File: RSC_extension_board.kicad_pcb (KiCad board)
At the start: 2 copper layers, 35 parts, among them J1 Conn_01x03, J10 Conn_01x02, J13 Conn_01x03, J14 500SSP1S2M2QEA, J16 Conn_01x10, J2 Conn_01x03, J3 Raspberry_Pi_4, J4 Conn_01x04, J5 Conn_01x03, J6 Conn_01x02, J7 Conn_01x03, J8 PRT-14417, J9 USB_C_Receptacle_PowerOnly_6P, Q1 BSS138, Q2 2N7002-7-F, U1 USBLC6-2SC6

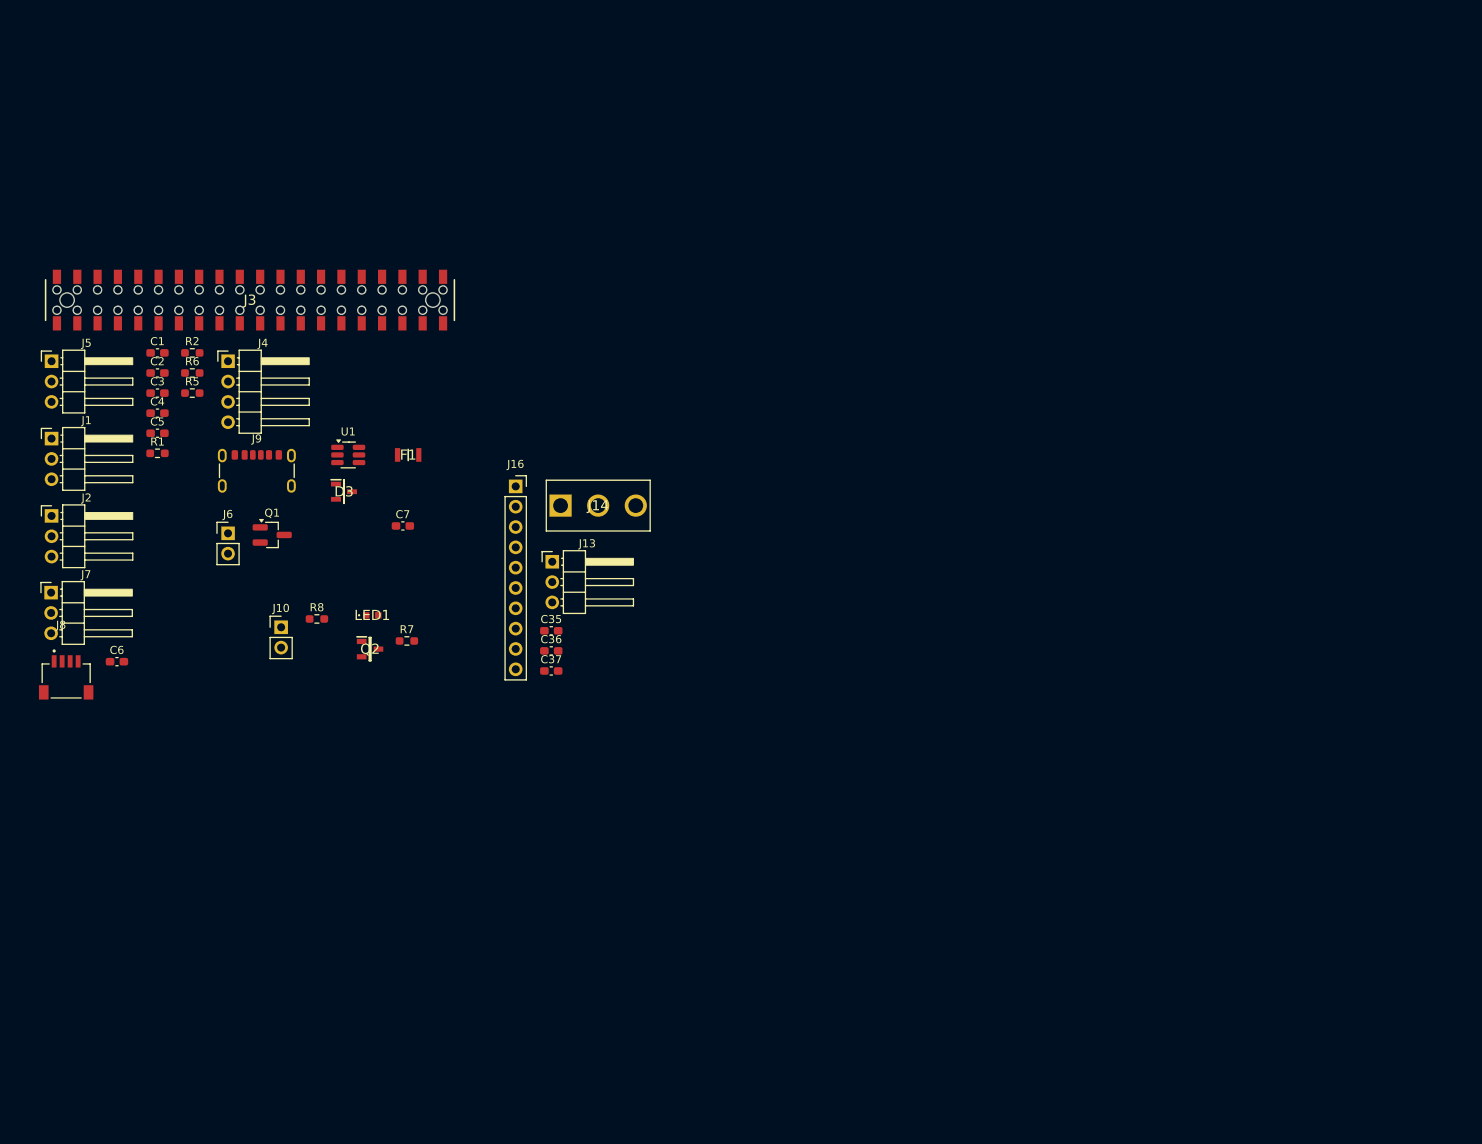
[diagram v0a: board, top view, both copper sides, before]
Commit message: annotation and pcb outline
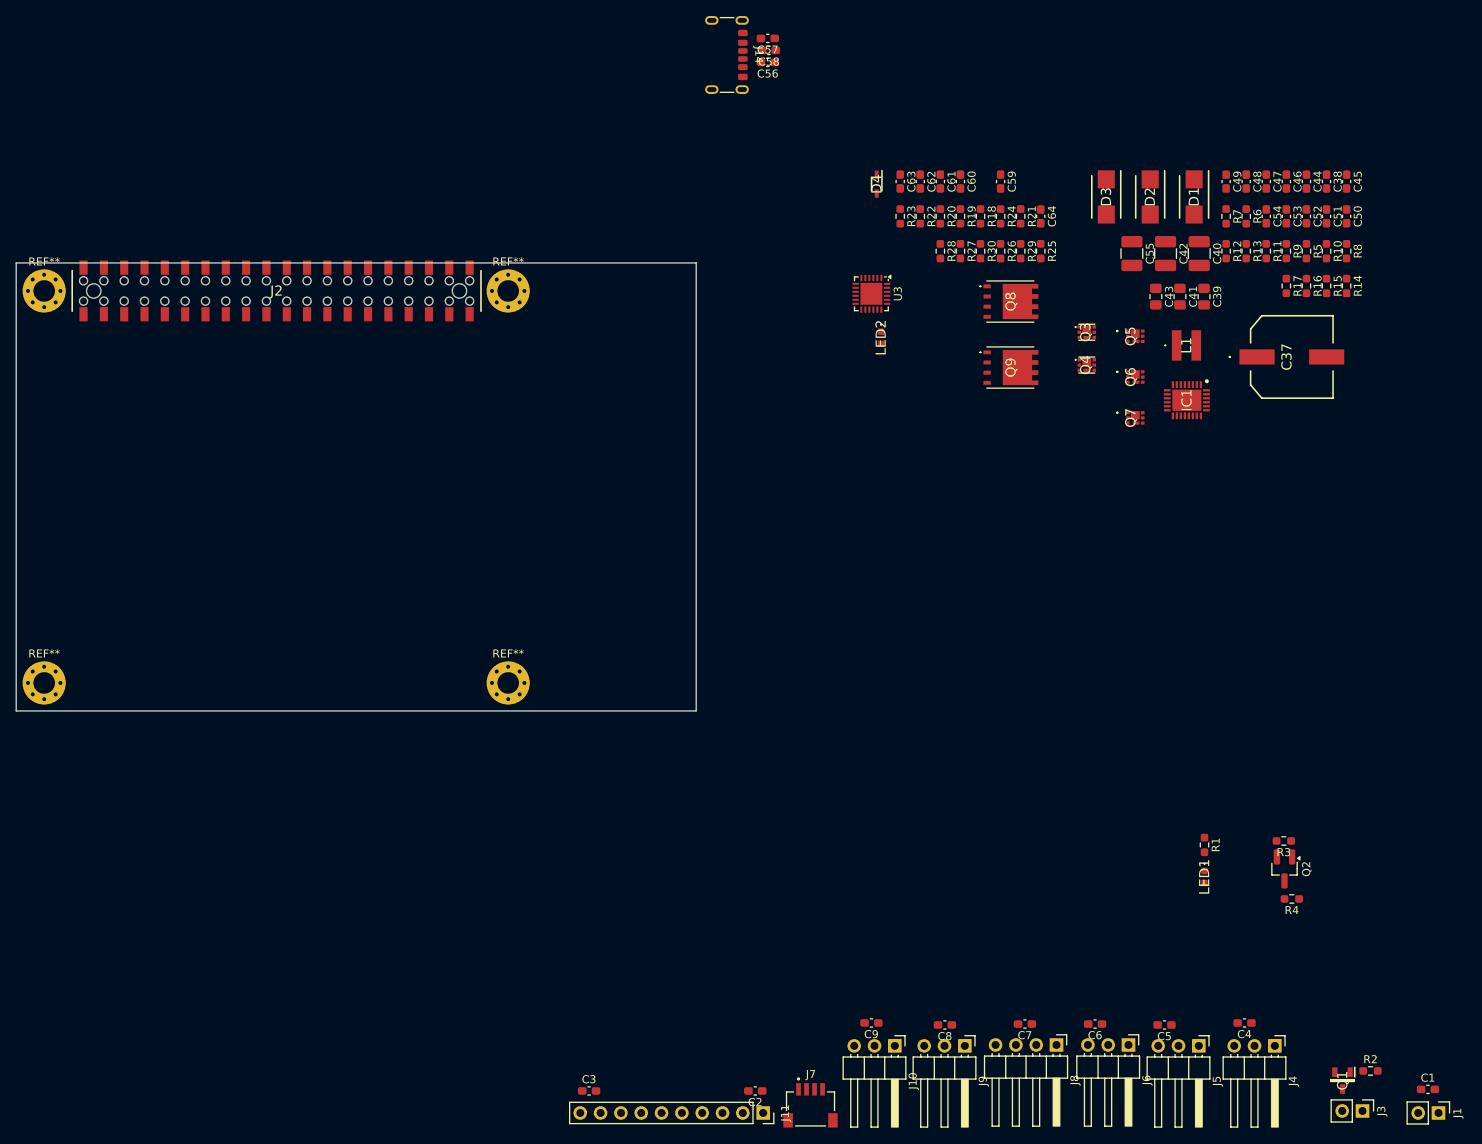
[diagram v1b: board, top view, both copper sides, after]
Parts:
- removed the C7 at (143.3, 77.9)
- removed F1: PTSLR08058V350, PTSLR08058V350:FUSC2516X100N
- removed the J9 at (125.1, 72.1)
- removed U1: USBLC6-2SC6, Package_TO_SOT_SMD:SOT-23-6_Handsoldering
- added C37: 50SVPF68M, 50SVPF68M:16SVF1000M, F.Cu at (254.5, 56.8)
- added C38: 15nF, Capacitor_SMD:C_0603_1608Metric_Pad1.08x0.95mm_HandSolder, F.Cu at (258.8, 34.8)
- added C39: 3.9nF, Capacitor_SMD:C_0805_2012Metric_Pad1.18x1.45mm_HandSolder, F.Cu at (243.5, 49.2)
- added C40: 22uF, Inductor_SMD:L_1210_3225Metric_Pad1.42x2.65mm_HandSolder, F.Cu at (242.9, 43.8)
- added C41: 3.9nF, Capacitor_SMD:C_0805_2012Metric_Pad1.18x1.45mm_HandSolder, F.Cu at (240.5, 49.2)
- added C42: 22uF, Inductor_SMD:L_1210_3225Metric_Pad1.42x2.65mm_HandSolder, F.Cu at (238.7, 43.8)
- added C43: 3.9nF, Capacitor_SMD:C_0805_2012Metric_Pad1.18x1.45mm_HandSolder, F.Cu at (237.5, 49.2)
- added C44: 1nF, Capacitor_SMD:C_0603_1608Metric_Pad1.08x0.95mm_HandSolder, F.Cu at (256.3, 34.8)
- added C45: 100nF, Capacitor_SMD:C_0603_1608Metric_Pad1.08x0.95mm_HandSolder, F.Cu at (261.3, 34.8)
- added C46: 47pF, Capacitor_SMD:C_0603_1608Metric_Pad1.08x0.95mm_HandSolder, F.Cu at (253.8, 34.8)
- added C47: 47pF, Capacitor_SMD:C_0603_1608Metric_Pad1.08x0.95mm_HandSolder, F.Cu at (251.3, 34.8)
- added C48: 100nF, Capacitor_SMD:C_0603_1608Metric_Pad1.08x0.95mm_HandSolder, F.Cu at (248.8, 34.8)
- added C49: 100nF, Capacitor_SMD:C_0603_1608Metric_Pad1.08x0.95mm_HandSolder, F.Cu at (246.2, 34.8)
- added C50: 100nF, Capacitor_SMD:C_0603_1608Metric_Pad1.08x0.95mm_HandSolder, F.Cu at (261.3, 39.2)
- added C51: 1uF, Capacitor_SMD:C_0603_1608Metric_Pad1.08x0.95mm_HandSolder, F.Cu at (258.8, 39.2)
- added C52: 22uF, Capacitor_SMD:C_0603_1608Metric_Pad1.08x0.95mm_HandSolder, F.Cu at (256.3, 39.2)
- added C53: 22uF, Capacitor_SMD:C_0603_1608Metric_Pad1.08x0.95mm_HandSolder, F.Cu at (253.8, 39.2)
- added C54: 22uF, Capacitor_SMD:C_0603_1608Metric_Pad1.08x0.95mm_HandSolder, F.Cu at (251.3, 39.2)
- added C55: 47uF, Inductor_SMD:L_1210_3225Metric_Pad1.42x2.65mm_HandSolder, F.Cu at (234.5, 43.8)
- added C56: 390pF, Capacitor_SMD:C_0603_1608Metric_Pad1.08x0.95mm_HandSolder, F.Cu at (188.9, 19.9)
- added C57: 3.3uF, Capacitor_SMD:C_0603_1608Metric_Pad1.08x0.95mm_HandSolder, F.Cu at (188.9, 16.9)
- added C58: 390pF, Capacitor_SMD:C_0603_1608Metric_Pad1.08x0.95mm_HandSolder, F.Cu at (189.1, 18.4)
- added C59: 1uF, Capacitor_SMD:C_0603_1608Metric_Pad1.08x0.95mm_HandSolder, F.Cu at (218.1, 34.8)
- added C60: 1uF, Capacitor_SMD:C_0603_1608Metric_Pad1.08x0.95mm_HandSolder, F.Cu at (213.0, 34.8)
- added C61: 1uF, Capacitor_SMD:C_0603_1608Metric_Pad1.08x0.95mm_HandSolder, F.Cu at (210.5, 34.8)
- added C62: 100nF, Capacitor_SMD:C_0603_1608Metric_Pad1.08x0.95mm_HandSolder, F.Cu at (208.0, 34.8)
- added C63: 100nF, Capacitor_SMD:C_0603_1608Metric_Pad1.08x0.95mm_HandSolder, F.Cu at (205.5, 34.8)
- added C64: 1uF, Capacitor_SMD:C_0603_1608Metric_Pad1.08x0.95mm_HandSolder, F.Cu at (223.1, 39.2)
- added D1: B220-13-F, B220-13-F:DIOM5336X250N, F.Cu at (242.2, 36.8)
- added D2: B220-13-F, B220-13-F:DIOM5336X250N, F.Cu at (236.8, 36.8)
- added D4: BAT54WS-7-F, BAT54WS-7-F:SOD2513X120N, F.Cu at (202.6, 35.1)
- added IC1: LM34936RHFR, LM34936RHFR:QFN50P400X500X100-29N-D, F.Cu at (241.3, 62.2)
- added L1: 74439323010, 74439323010:74439323010, F.Cu at (241.3, 55.3)
- added LED2: KR_EELP41.22-Q1S1-36-A8J8-020-R18, KR_EELP41.22-Q1S1-36-A8J8-020-R18:KREELP4122Q1S136A8J8020R18, F.Cu at (203.1, 54.3)
- added Q3: CSD17571Q2, CSD17571Q2:CSD25302Q2, F.Cu at (228.7, 53.7)
- added Q4: CSD17571Q2, CSD17571Q2:CSD25302Q2, F.Cu at (228.7, 57.8)
- added Q5: CSD15571Q2, CSD15571Q2:CSD15571Q2, F.Cu at (234.9, 54.2)
- added Q6: CSD15571Q2, CSD15571Q2:CSD15571Q2, F.Cu at (234.9, 59.3)
- added Q7: CSD15571Q2, CSD15571Q2:CSD15571Q2, F.Cu at (234.9, 64.4)
- added Q8: BSC084P03NS3GATMA1, BSC084P03NS3GATMA1:BSC054N04NSG, F.Cu at (222.0, 49.8)
- added Q9: BSC084P03NS3GATMA1, BSC084P03NS3GATMA1:BSC054N04NSG, F.Cu at (222.0, 58.1)
- added R10: 10, Resistor_SMD:R_0603_1608Metric_Pad0.98x0.95mm_HandSolder, F.Cu at (258.8, 43.5)
- added R11: 23k7, Resistor_SMD:R_0603_1608Metric_Pad0.98x0.95mm_HandSolder, F.Cu at (251.3, 43.5)
- added R12: 100, Resistor_SMD:R_0603_1608Metric_Pad0.98x0.95mm_HandSolder, F.Cu at (246.2, 43.5)
- added R13: 100, Resistor_SMD:R_0603_1608Metric_Pad0.98x0.95mm_HandSolder, F.Cu at (248.8, 43.5)
- added R14: 0.01, Resistor_SMD:R_0603_1608Metric_Pad0.98x0.95mm_HandSolder, F.Cu at (261.3, 47.9)
- added R15: 10k, Resistor_SMD:R_0603_1608Metric_Pad0.98x0.95mm_HandSolder, F.Cu at (258.8, 47.9)
- added R16: 105k, Resistor_SMD:R_0603_1608Metric_Pad0.98x0.95mm_HandSolder, F.Cu at (256.3, 47.9)
- added R17: 20k, Resistor_SMD:R_0603_1608Metric_Pad0.98x0.95mm_HandSolder, F.Cu at (253.8, 47.9)
- added R18: 10k, Resistor_SMD:R_0603_1608Metric_Pad0.98x0.95mm_HandSolder, F.Cu at (215.5, 39.2)
- added R19: 5k1, Resistor_SMD:R_0603_1608Metric_Pad0.98x0.95mm_HandSolder, F.Cu at (213.0, 39.2)
- added R20: 2k4, Resistor_SMD:R_0603_1608Metric_Pad0.98x0.95mm_HandSolder, F.Cu at (210.5, 39.2)
- added R21: 1k, Resistor_SMD:R_0603_1608Metric_Pad0.98x0.95mm_HandSolder, F.Cu at (220.6, 39.2)
- added R22: DNP, Resistor_SMD:R_0603_1608Metric_Pad0.98x0.95mm_HandSolder, F.Cu at (208.0, 39.2)
- added R23: 0, Resistor_SMD:R_0603_1608Metric_Pad0.98x0.95mm_HandSolder, F.Cu at (205.5, 39.2)
- added R24: 49k9, Resistor_SMD:R_0603_1608Metric_Pad0.98x0.95mm_HandSolder, F.Cu at (218.1, 39.2)
- added R25: 5k1, Resistor_SMD:R_0603_1608Metric_Pad0.98x0.95mm_HandSolder, F.Cu at (223.1, 43.5)
- added R26: 5k1, Resistor_SMD:R_0603_1608Metric_Pad0.98x0.95mm_HandSolder, F.Cu at (218.1, 43.5)
- added R27: 50k, Resistor_SMD:R_0603_1608Metric_Pad0.98x0.95mm_HandSolder, F.Cu at (213.0, 43.5)
- added R28: 68, Resistor_SMD:R_0603_1608Metric_Pad0.98x0.95mm_HandSolder, F.Cu at (210.5, 43.5)
- added R29: DNP, Resistor_SMD:R_0603_1608Metric_Pad0.98x0.95mm_HandSolder, F.Cu at (220.6, 43.5)
- added R30: 0, Resistor_SMD:R_0603_1608Metric_Pad0.98x0.95mm_HandSolder, F.Cu at (215.5, 43.5)
- added R7: 105k, Resistor_SMD:R_0603_1608Metric_Pad0.98x0.95mm_HandSolder, F.Cu at (246.2, 39.2)
- added R8: 2k, Resistor_SMD:R_0603_1608Metric_Pad0.98x0.95mm_HandSolder, F.Cu at (261.3, 43.5)
- added R9: 93k1, Resistor_SMD:R_0603_1608Metric_Pad0.98x0.95mm_HandSolder, F.Cu at (253.8, 43.5)
- added REF**: MountingHole_2.7mm_Pad_Via, MountingHole:MountingHole_2.7mm_Pad_Via, F.Cu at (156.5, 48.5)
- added REF**: MountingHole_2.7mm_Pad_Via, MountingHole:MountingHole_2.7mm_Pad_Via, F.Cu at (156.5, 97.5)
- added REF**: MountingHole_2.7mm_Pad_Via, MountingHole:MountingHole_2.7mm_Pad_Via, F.Cu at (98.5, 97.5)
- added REF**: MountingHole_2.7mm_Pad_Via, MountingHole:MountingHole_2.7mm_Pad_Via, F.Cu at (98.5, 48.5)
- added U3: CYPD3177-24LQ, Package_DFN_QFN:QFN-24-1EP_4x4mm_P0.5mm_EP2.75x2.75mm, F.Cu at (201.9, 48.9)
- D3: value CDSOT23-T05 -> B220-13-F; footprint CDSOT23-T05:SOT95P230X117-3N -> B220-13-F:DIOM5336X250N
- J14: value 500SSP1S2M2QEA -> USB_C_Receptacle_PowerOnly_6P; footprint 500SSP1S2M2QEA:500SSP1S2M2QEA -> Connector_USB:USB_C_Receptacle_GCT_USB4125-xx-x-0190_6P_TopMnt_Horizontal
- R5: value 5.1k -> 1k21
- R6: value 5.1k -> 249k
- moved C1 178.7 mm to (271.5, 148.3)
- moved J4 170.7 mm to (252.3, 142.9), turned to -90 degrees
- moved J1 167.8 mm to (272.8, 151.2), turned to -90 degrees
- moved C4 159.6 mm to (248.5, 140.0), turned to 180 degrees
- moved J5 158.0 mm to (242.8, 142.9), turned to -90 degrees
- moved R4 153.5 mm to (254.5, 124.5), turned to 180 degrees
- moved C5 150.0 mm to (238.5, 140.2), turned to 180 degrees
- moved R3 148.9 mm to (253.5, 117.2), turned to 180 degrees
- moved J3 148.1 mm to (263.3, 151.0), turned to -90 degrees
- moved R2 143.3 mm to (264.3, 146.0)
- moved J9 142.7 mm to (213.6, 142.9), turned to -90 degrees
- moved R5 140.4 mm to (256.3, 43.5), turned to -90 degrees
- moved J8 134.3 mm to (225.0, 142.8), turned to -90 degrees
- moved C7 134.1 mm to (221.1, 140.1), turned to 180 degrees
- moved Q2 133.2 mm to (253.5, 120.8), turned to -90 degrees
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- renumbered C5 to C1, C36 to C2, C37 to C3, C1 to C4, C2 to C5, C35 to C6, C3 to C7, C4 to C8, C6 to C9, J6 to J1, J7 to J10, J16 to J11, J3 to J2, J10 to J3, J1 to J4, J2 to J5, J13 to J6, J8 to J7, J4 to J8, J5 to J9, Q2 to Q1, Q1 to Q2, R7 to R1, R8 to R2, R1 to R3, R2 to R4
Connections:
- C1 pad 1: Earth -> GND
- C2 pad 2: Earth -> GND
- C3 pad 2: Earth -> GND
- C4 pad 2: Earth -> GND
- C5 pad 2: Earth -> GND
- C6 pad 2: Earth -> GND
- C7 pad 2: Earth -> GND
- C8 pad 2: Earth -> GND
- C9 pad 2: Earth -> GND
- D3 pad 1: Earth -> Net-(D3-K)
- D3 pad 2: Earth -> Net-(D2-A)
- J10 pad 3: Earth -> GND
- J11 pad 2: Earth -> GND
- J2 pad 14: Earth -> GND
- J2 pad 20: Earth -> GND
- J2 pad 24: /SPI_CS -> unconnected-(J2-~{CE0}_SPI0/GPIO08-Pad24)
- J2 pad 25: Earth -> GND
- J2 pad 26: unconnected-(J3-~{CE1}_SPI0/GPIO07-Pad26) -> /SPI_CS
- J2 pad 30: Earth -> GND
- J2 pad 34: Earth -> GND
- J2 pad 39: Earth -> GND
- J2 pad 6: Earth -> GND
- J2 pad 9: Earth -> GND
- J4 pad 3: Earth -> GND
- J5 pad 3: Earth -> GND
- J6 pad 3: Earth -> GND
- J7 pad 1: Earth -> /SCL
- J7 pad 2: +3.3V -> /SDA
- J7 pad 3: /SDA -> +3.3V
- J7 pad 4: /SCL -> GND
- J7 pad S1: Earth -> (no net)
- J7 pad S2: Earth -> (no net)
- J8 pad 4: Earth -> GND
- J9 pad 3: Earth -> GND
- LED1 pad 1: Earth -> GND
- Q1 pad 2: Earth -> GND
- R5 pad 2: Earth -> GND
- R6 pad 1: Net-(R6-Pad1) -> VBUS
- R6 pad 2: Earth -> Net-(IC1-EN/UVLO)
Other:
- board outline added: 85 x 56 mm

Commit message: ...
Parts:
- moved C64 122.6 mm to (101.6, 56.1), turned to 0 degrees
- moved Q8 121.2 mm to (102.1, 67.8), turned to 0 degrees
- moved Q9 120.0 mm to (102.1, 64.0), turned to 180 degrees
- moved R18 118.2 mm to (103.1, 75.6), turned to 180 degrees
- moved C60 117.7 mm to (103.2, 77.1), turned to 180 degrees
- moved R21 116.8 mm to (110.1, 77.2), turned to 90 degrees
- moved R24 114.2 mm to (107.4, 67.1), turned to 180 degrees
- moved R25 112.1 mm to (113.7, 68.0), turned to 180 degrees
- moved R28 111.2 mm to (106.3, 82.5), turned to 0 degrees
- moved R27 109.5 mm to (110.6, 82.2), turned to 90 degrees
- moved R29 108.9 mm to (113.7, 64.5), turned to 180 degrees
- moved C59 108.9 mm to (119.1, 80.2)
- moved R19 105.5 mm to (113.8, 75.2), turned to 180 degrees
- moved C57 104.0 mm to (116.2, 91.2), turned to -90 degrees
- moved R26 103.8 mm to (117.2, 68.0), turned to 180 degrees
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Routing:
- net GND: track 0.00 -> 1.50 mm

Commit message: new caps and bit of layout
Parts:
- added C39: 25SVPF47M, 25SVPF47M:16SVF180M, F.Cu at (129.1, 131.9)
- C37: value 50SVPF68M -> 25SVPF47M; footprint 50SVPF68M:16SVF1000M -> 25SVPF47M:16SVF180M
- J2: moved to B.Cu
- moved J8 251.2 mm to (40.8, -28.0)
- moved C7 248.8 mm to (40.1, -30.5)
- moved R4 232.5 mm to (117.5, -54.9), turned to -90 degrees
- moved Q2 231.1 mm to (114.0, -55.0), turned to 0 degrees
- moved R3 230.4 mm to (110.5, -54.8), turned to -90 degrees
- moved C3 214.1 mm to (45.4, -28.0)
- moved J11 214.1 mm to (67.2, -25.2)
- moved C2 214.0 mm to (66.4, -28.0)
- moved J10 212.9 mm to (111.5, -48.5)
- moved J9 212.9 mm to (120.2, -48.5)
- moved C8 212.1 mm to (119.4, -51.0)
- moved C9 211.7 mm to (110.6, -51.0)
- moved J1 186.9 mm to (126.6, 34.8)
- moved C1 186.6 mm to (125.3, 32.2)
- moved J3 174.8 mm to (132.8, 34.8)
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- renumbered C39 to C40, C40 to C42, C42 to C44, C44 to C45, C45 to C46, C46 to C47, C47 to C48, C48 to C49, C49 to C50, C50 to C51, C51 to C52, C52 to C53, C53 to C54, C54 to C55, C55 to C56, C56 to C57, C57 to C58, C58 to C59, C59 to C60, C60 to C61, C61 to C62, C62 to C63, C63 to C64, C64 to C65, R8 to R10, R9 to R8, R10 to R9
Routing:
- net Net-(Q4-S-Pad4): track 0.00 -> 1.81 mm
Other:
- board size 85 x 56 mm -> 65 x 56 mm

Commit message: layout- 1st placement
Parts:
- J10, J4, J5, J6, J9: footprint Connector_PinHeader_2.54mm:PinHeader_1x03_P2.54mm_Horizontal -> Connector_PinHeader_2.54mm:PinHeader_1x03_P2.54mm_Vertical
- J2: moved to F.Cu
- J8: footprint Connector_PinHeader_2.54mm:PinHeader_1x04_P2.54mm_Horizontal -> Connector_PinHeader_2.54mm:PinHeader_1x04_P2.54mm_Vertical
- moved J8 121.7 mm to (119.0, 65.2)
- moved C7 121.6 mm to (118.1, 62.8)
- moved C8 119.9 mm to (143.4, 66.5)
- moved C9 119.9 mm to (134.7, 66.5)
- moved J10 119.9 mm to (135.5, 69.0)
- moved J9 119.9 mm to (144.3, 69.0)
- moved Q2 119.9 mm to (138.0, 62.5)
- moved R3 119.9 mm to (134.5, 62.7)
- moved R4 119.9 mm to (141.5, 62.6)
- moved C2 111.5 mm to (125.9, 66.2)
- moved C3 111.5 mm to (104.9, 66.2)
- moved J11 111.5 mm to (126.7, 69.0)
- moved J4 83.1 mm to (96.8, 58.4), turned to 180 degrees
- moved C4 75.4 mm to (99.2, 54.9), turned to 90 degrees
- moved J5 53.1 mm to (158.2, 53.5), turned to 0 degrees
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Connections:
- REF** pad 1: (no net) -> GND (x3)

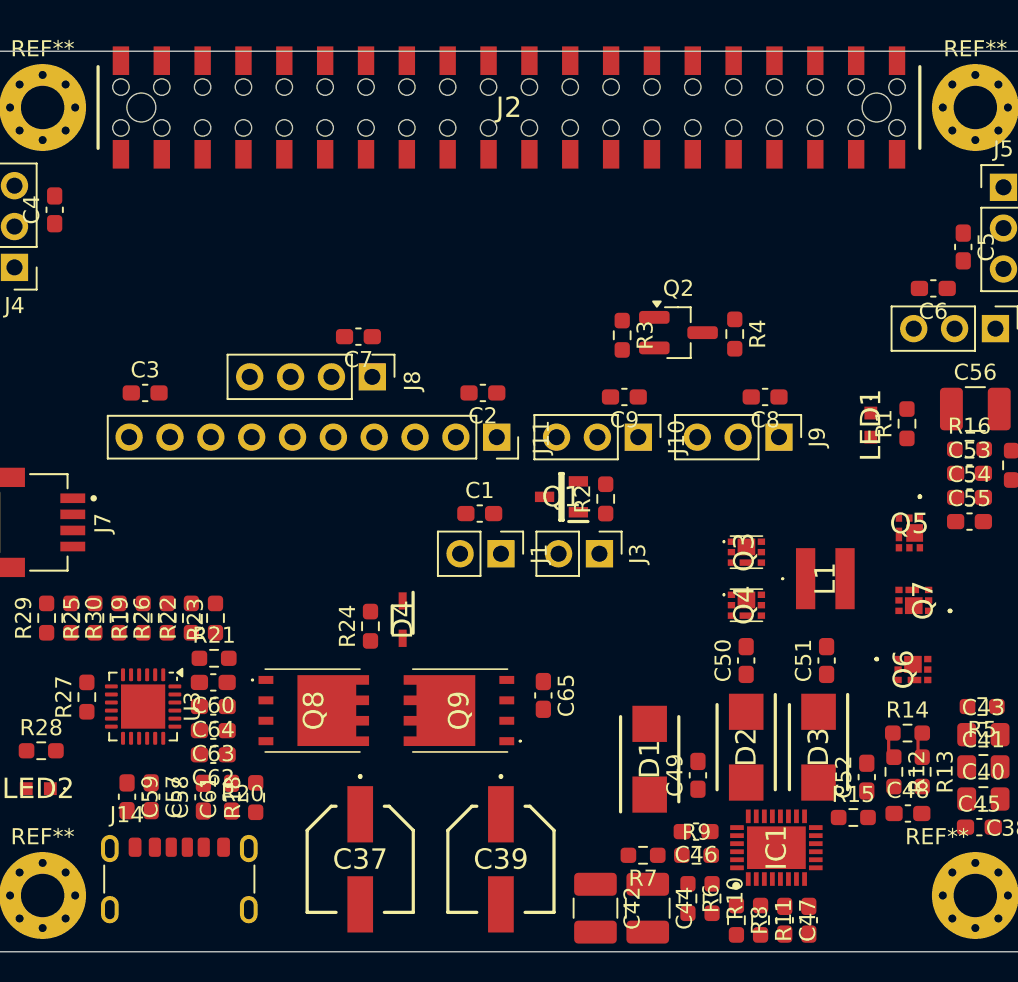
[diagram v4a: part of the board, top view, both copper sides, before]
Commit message: new bottom layer footprint for Pi connector
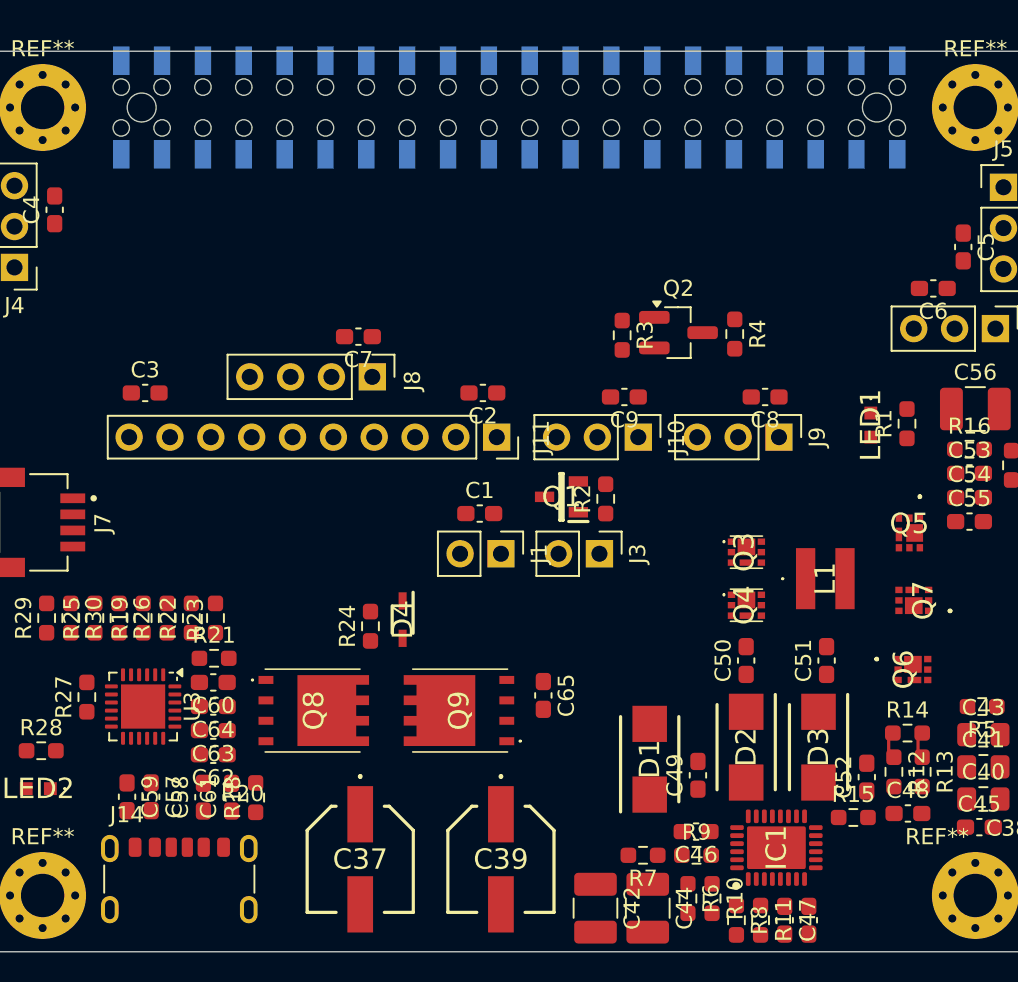
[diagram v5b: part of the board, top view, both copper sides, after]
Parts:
- J2: footprint KiCad:M207812045R -> KiCad:M207812045R_bottomLayer; moved to B.Cu
- turned J2 to 180 degrees
